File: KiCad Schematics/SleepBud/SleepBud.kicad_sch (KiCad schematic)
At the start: 159 parts, among them J1 12V Barrel Jack, J2 USB_B_Micro, J3 Button Connector, J4 AM312 Connector, J5 LED Lamp Connector, J6 Connector to Buzzer, Q1 FQP27P06, Q2 AO3400A, SW1 EN Button, SW2 Reset Button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

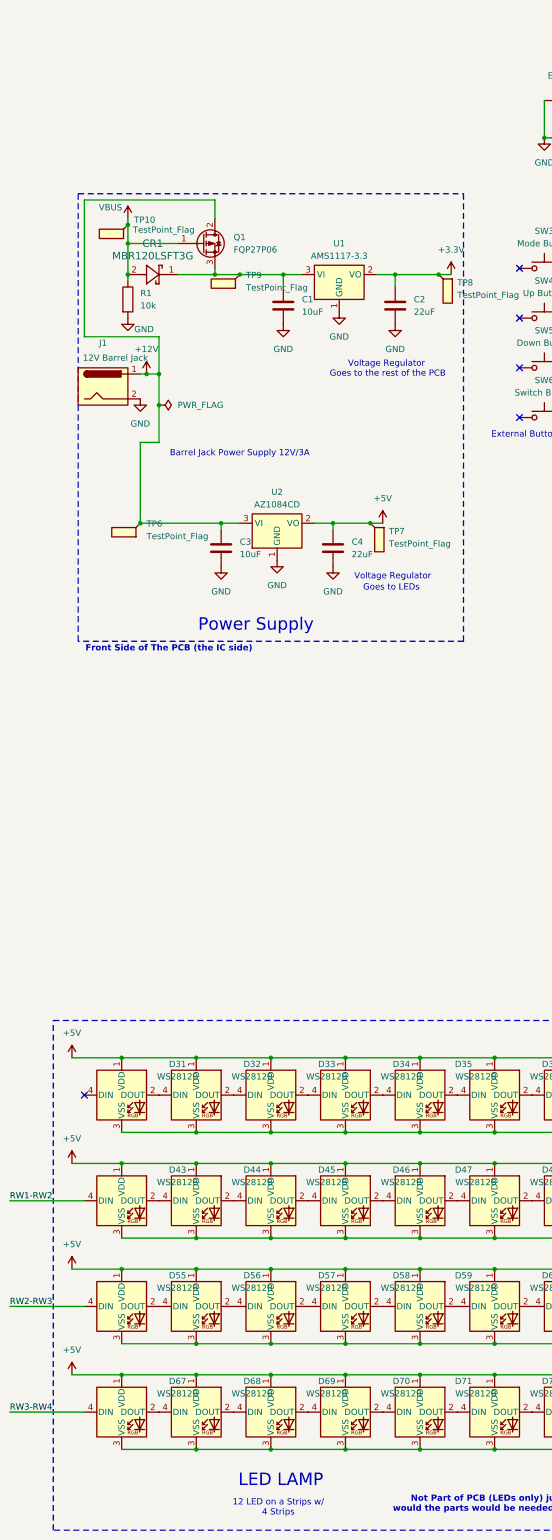
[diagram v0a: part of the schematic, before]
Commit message: Changed PMosfet
Change the Mosfet can be seen on schematic and PCB layout
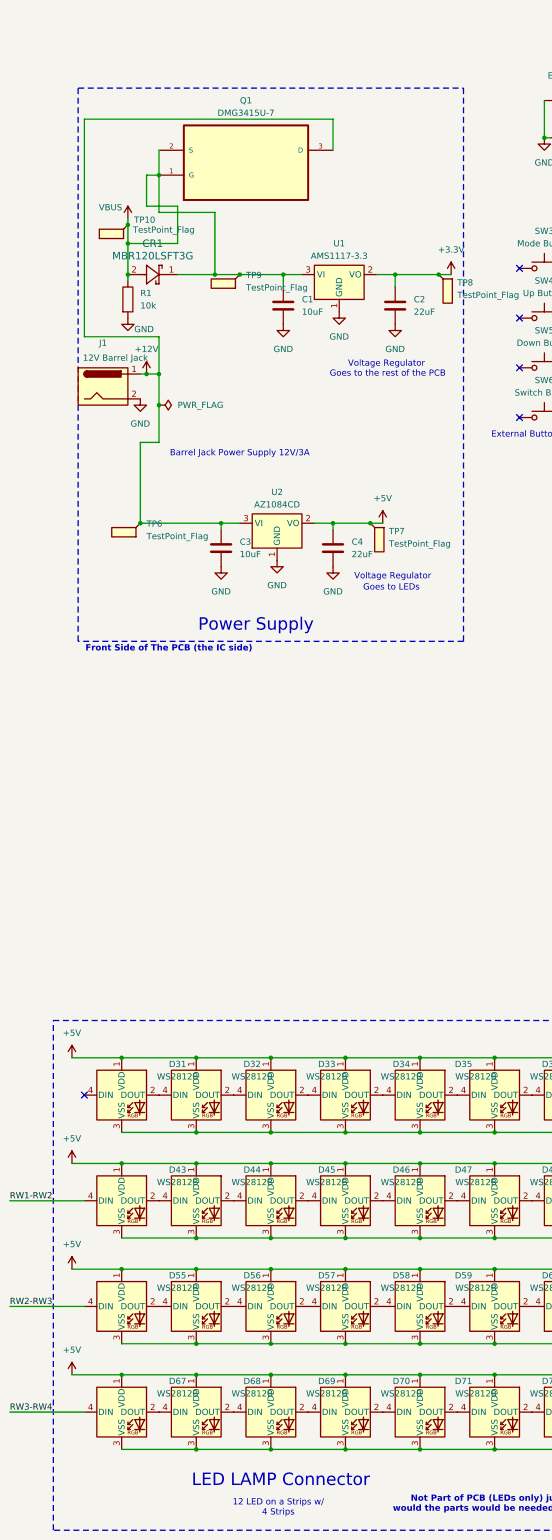
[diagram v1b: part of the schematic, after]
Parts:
- removed Q1: FQP27P06, Package_TO_SOT_THT:TO-220-3_Vertical, symbol Transistor_FET:FQP27P06
- added Q1: DMG3415U-7, DMG3415U_7:SOT95P240X105-3N, symbol DMG3415U-7:DMG3415U-7
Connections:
- net +12V: now also Q1.3 (D)
- net VBUS: now also C1.1, CR1.1, TP9.1, U1.3 (VI), Q1.1 (G), Q1.2 (S)
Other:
- note added: "LED LAMP Connector"
- note removed: "LED LAMP"
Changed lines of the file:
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@@
 	)
 	(junction
+		(at 46.99 125.73)
+		(diameter 0)
+		(color 0 0 0 0)
+	)
+	(junction
 		(at 152.4 91.44)
 		(diameter 0)
@@
 	(wire
 		(pts
+			(xy 50.8 132.08) (xy 44.45 132.08)
+		)
+		(stroke
+			(width 0)
+			(type default)
+		)
+	)
+	(wire
+		(pts
 			(xy 504.19 316.23) (xy 519.43 316.23)
 		)
@@
 	(wire
 		(pts
-			(xy 31.75 158.75) (xy 31.75 130.81)
-		)
-		(stroke
-			(width 0)
-			(type default)
-		)
-	)
-	(wire
-		(pts
 			(xy 58.42 146.05) (xy 63.5 146.05)
 		)
@@
 	(wire
 		(pts
+			(xy 31.75 114.3) (xy 82.55 114.3)
+		)
+		(stroke
+			(width 0)
+			(type default)
+		)
+	)
+	(wire
+		(pts
 			(xy 316.23 200.66) (xy 303.53 200.66)
 		)
@@
 	(wire
 		(pts
-			(xy 31.75 130.81) (xy 58.42 130.81)
+			(xy 302.26 198.12) (xy 302.26 207.01)
 		)
 		(stroke
@@
 	(wire
 		(pts
-			(xy 302.26 198.12) (xy 302.26 207.01)
+			(xy 100.33 342.9) (xy 115.57 342.9)
 		)
 		(stroke
@@
 	(wire
 		(pts
-			(xy 100.33 342.9) (xy 115.57 342.9)
+			(xy 161.29 349.25) (xy 176.53 349.25)
 		)
 		(stroke
@@
 	(wire
 		(pts
-			(xy 161.29 349.25) (xy 176.53 349.25)
+			(xy 58.42 133.35) (xy 58.42 146.05)
 		)
 		(stroke
@@
 	(wire
 		(pts
+			(xy 46.99 133.35) (xy 58.42 133.35)
+		)
+		(stroke
+			(width 0)
+			(type default)
+		)
+	)
+	(wire
+		(pts
 			(xy 46.99 158.75) (xy 31.75 158.75)
 		)
@@
 	(wire
 		(pts
+			(xy 44.45 132.08) (xy 44.45 125.73)
+		)
+		(stroke
+			(width 0)
+			(type default)
+		)
+	)
+	(wire
+		(pts
 			(xy 323.85 171.45) (xy 323.85 180.34)
 		)
@@
 	(wire
 		(pts
+			(xy 46.99 120.65) (xy 46.99 125.73)
+		)
+		(stroke
+			(width 0)
+			(type default)
+		)
+	)
+	(wire
+		(pts
 			(xy 137.16 110.49) (xy 139.7 110.49)
 		)
@@
 	(wire
 		(pts
+			(xy 44.45 125.73) (xy 46.99 125.73)
+		)
+		(stroke
+			(width 0)
+			(type default)
+		)
+	)
+	(wire
+		(pts
 			(xy 229.87 147.32) (xy 248.92 147.32)
 		)
@@
 	(wire
 		(pts
+			(xy 31.75 114.3) (xy 31.75 158.75)
+		)
+		(stroke
+			(width 0)
+			(type default)
+		)
+	)
+	(wire
+		(pts
 			(xy 130.81 327.66) (xy 146.05 327.66)
 		)
@@
 	(wire
 		(pts
-			(xy 220.98 176.53) (xy 220.98 138.43)
+			(xy 50.8 139.7) (xy 50.8 132.08)
 		)
 		(stroke
@@
 	(wire
 		(pts
-			(xy 213.36 115.57) (xy 213.36 92.71)
+			(xy 220.98 176.53) (xy 220.98 138.43)
 		)
 		(stroke
@@
 	(wire
 		(pts
-			(xy 336.55 200.66) (xy 364.49 200.66)
+			(xy 213.36 115.57) (xy 213.36 92.71)
 		)
 		(stroke
@@
 	(wire
 		(pts
-			(xy 58.42 144.78) (xy 58.42 146.05)
+			(xy 336.55 200.66) (xy 364.49 200.66)
 		)
 		(stroke
@@
 	(wire
 		(pts
-			(xy 69.85 349.25) (xy 85.09 349.25)
+			(xy 46.99 125.73) (xy 46.99 133.35)
 		)
 		(stroke
@@
 	(wire
 		(pts
-			(xy 157.48 133.35) (xy 157.48 152.4)
+			(xy 69.85 349.25) (xy 85.09 349.25)
 		)
 		(stroke
@@
 	(wire
 		(pts
-			(xy 180.34 200.66) (xy 180.34 156.21)
+			(xy 157.48 133.35) (xy 157.48 152.4)
 		)
 		(stroke
@@
 	(wire
 		(pts
-			(xy 443.23 300.99) (xy 458.47 300.99)
+			(xy 180.34 200.66) (xy 180.34 156.21)
 		)
 		(stroke
@@
 	(wire
 		(pts
-			(xy 213.36 199.39) (xy 218.44 199.39)
+			(xy 443.23 300.99) (xy 458.47 300.99)
 		)
 		(stroke
@@
 	(wire
 		(pts
-			(xy 427.99 300.99) (xy 443.23 300.99)
+			(xy 213.36 199.39) (xy 218.44 199.39)
 		)
 		(stroke
@@
 	(wire
 		(pts
-			(xy 248.92 154.94) (xy 248.92 151.13)
+			(xy 427.99 300.99) (xy 443.23 300.99)
 		)
 		(stroke
@@
 	(wire
 		(pts
-			(xy 58.42 130.81) (xy 58.42 134.62)
+			(xy 248.92 154.94) (xy 248.92 151.13)
 		)
 		(stroke
@@
 	(wire
 		(pts
+			(xy 82.55 114.3) (xy 82.55 120.65)
+		)
+		(stroke
+			(width 0)
+			(type default)
+		)
+	)
+	(wire
+		(pts
 			(xy 219.71 140.97) (xy 219.71 187.96)
 		)
@@
 	)
 	(rectangle
-		(start 30.48 129.54)
+		(start 30.48 107.95)
 		(end 109.22 220.98)
 		(stroke
@@
 		)
 	)
-	(text "LED LAMP"
+	(text "LED LAMP Connector"
 		(exclude_from_sim no)
 		(at 71.882 392.43 0)
@@
 	)
 	(symbol
-		(lib_id "Transistor_FET:FQP27P06")
-		(at 55.88 139.7 0)
-		(unit 1)
-		(exclude_from_sim no)
-		(in_bom yes)
-		(on_board yes)
-		(dnp no)
-		(fields_autoplaced yes)
-		(property "Reference" "Q1"
-			(at 62.23 138.4299 0)
-			(effects
-				(font
-					(size 1.27 1.27)
-				)
-				(justify left)
-			)
-		)
-		(property "Value" "FQP27P06"
-			(at 62.23 140.9699 0)
-			(effects
-				(font
-					(size 1.27 1.27)
-				)
-				(justify left)
-			)
-		)
-		(property "Footprint" "Package_TO_SOT_THT:TO-220-3_Vertical"
-			(at 60.96 141.605 0)
-			(effects
-				(font
-					(size 1.27 1.27)
-					(italic yes)
-				)
-				(justify left)
-				(hide yes)
-			)
-		)
-		(property "Datasheet" "https://www.onsemi.com/pub/Collateral/FQP27P06-D.PDF"
-			(at 60.96 143.51 0)
-			(effects
-				(font
-					(size 1.27 1.27)
-				)
-				(justify left)
-				(hide yes)
-			)
-		)
-		(property "Description" "-27A Id, -60V Vds, QFET P-Channel MOSFET, TO-220"
-			(at 55.88 139.7 0)
-			(effects
-				(font
-					(size 1.27 1.27)
-				)
-				(hide yes)
-			)
-		)
-		(pin "1"
-		)
-		(pin "3"
-		)
-		(pin "2"
-		)
-		(instances
-			(project ""
-				(path "/976e55d6-47c8-4a6a-a3ac-d81121411704"
-					(reference "Q1")
-					(unit 1)
-				)
-			)
-		)
-	)
-	(symbol
 		(lib_id "JTAG Pads:JTAG_PAD")
 		(at 224.79 187.96 0)
@@
 					(unit 1)
 				)
+			)
+		)
+	)
+	(symbol
+		(lib_id "DMG3415U-7:DMG3415U-7")
+		(at 64.77 120.65 0)
+		(unit 1)
+		(exclude_from_sim no)
+		(in_bom yes)
+		(on_board yes)
+		(dnp no)
+		(fields_autoplaced yes)
+		(property "Reference" "Q1"
+			(at 64.77 110.49 0)
+			(effects
+				(font
+					(size 1.27 1.27)
+				)
+			)
+		)
+		(property "Value" "DMG3415U-7"
+			(at 64.77 113.03 0)
+			(effects
+				(font
+					(size 1.27 1.27)
+				)
+			)
+		)
+		(property "Footprint" "DMG3415U_7:SOT95P240X105-3N"
+			(at 64.77 120.65 0)
+			(effects
+				(font
+					(size 1.27 1.27)
+				)
+				(justify bottom)
+				(hide yes)
+			)
+		)
+		(property "Datasheet" ""
+			(at 64.77 120.65 0)
+			(effects
+				(font
+					(size 1.27 1.27)
+				)
+				(hide yes)
+			)
+		)
+		(property "Description" ""
+			(at 64.77 120.65 0)
+			(effects
+				(font
+					(size 1.27 1.27)
+				)
+				(hide yes)
+			)
+		)
+		(property "MPN" "DMG3415U-7"
+			(at 64.77 120.65 0)
+			(effects
+				(font
+					(size 1.27 1.27)
+				)
+				(justify bottom)
+				(hide yes)
+			)
+		)
+		(property "OC_FARNELL" "1843688"
+			(at 64.77 120.65 0)
+			(effects
+				(font
+					(size 1.27 1.27)
+				)
+				(justify bottom)
+				(hide yes)
+			)
+		)
+		(property "OC_NEWARK" "12T2026"
+			(at 64.77 120.65 0)
+			(effects
+				(font
+					(size 1.27 1.27)
+				)
+				(justify bottom)
+				(hide yes)
+			)
+		)
+		(property "SUPPLIER" "Diodes Inc"
+			(at 64.77 120.65 0)
+			(effects
+				(font
+					(size 1.27 1.27)
+				)
+				(justify bottom)
+				(hide yes)
+			)
+		)
+		(property "PACKAGE" "SOT-23-3"
+			(at 64.77 120.65 0)
+			(effects
+				(font
+					(size 1.27 1.27)
+				)
+				(justify bottom)
+				(hide yes)
+			)
+		)
+		(pin "3"
+		)
+		(pin "1"
+		)
+		(pin "2"
+		)
+		(instances
+			(project ""
+				(path "/976e55d6-47c8-4a6a-a3ac-d81121411704"
+					(reference "Q1")
+					(unit 1)
+				)

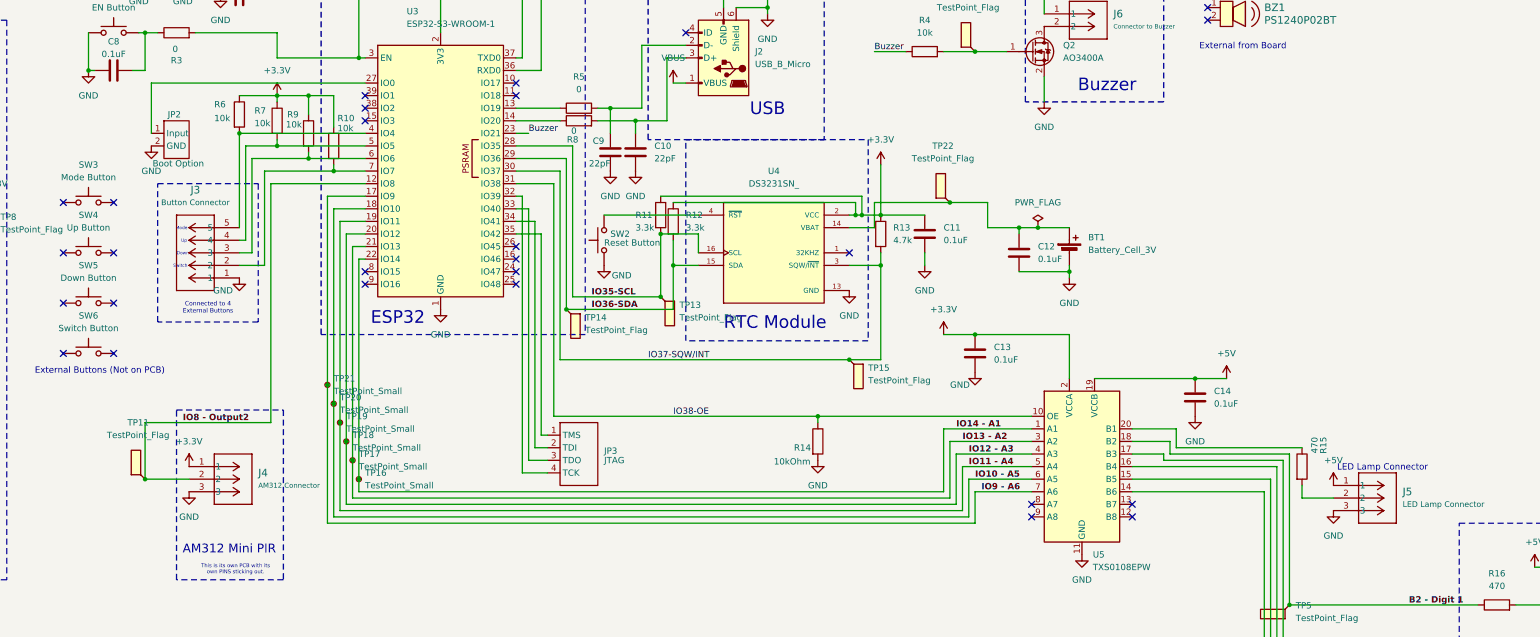
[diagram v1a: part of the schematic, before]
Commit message: Added Some Ground Vias to each Corner of the Board
Still missing the ground stitching for some components, will work on it it later
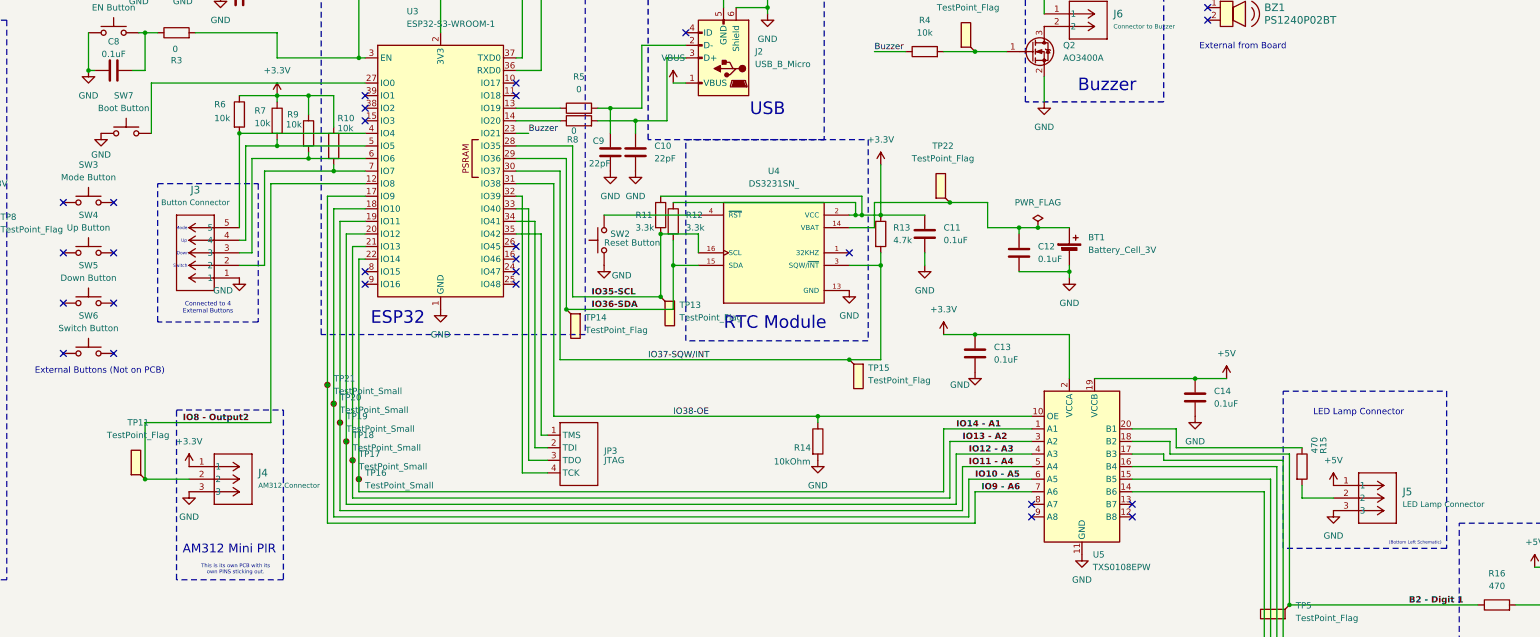
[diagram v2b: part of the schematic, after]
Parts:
- removed JP2: Boot Option, Connector_PinHeader_1.00mm:PinHeader_2x01_P1.00mm_Vertical_SMD, symbol Boot Option:Boot_Option
- added SW7: Boot Button, Button_Switch_SMD:SW_Tactile_SPST_NO_Straight_CK_PTS636Sx25SMTRLFS, symbol Switch:SW_Push
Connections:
- net GND: now also SW7.1
- net at U3.27 (IO0): now also SW7.2
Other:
- note added: "(Bottom Left Schematic)"
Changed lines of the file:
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@@
 	)
 	(rectangle
+		(start 367.03 182.88)
+		(end 400.05 214.63)
+		(stroke
+			(width 0)
+			(type dash_dot)
+		)
+		(fill
+			(type none)
+		)
+	)
+	(rectangle
 		(start 246.38 132.08)
 		(end 283.21 172.72)
@@
 	(text "LED Lamp Connector\n"
 		(exclude_from_sim no)
-		(at 387.096 198.374 0)
+		(at 382.27 187.198 0)
 		(effects
 			(font
@@
 		)
 	)
+	(text "(Bottom Left Schematic)"
+		(exclude_from_sim no)
+		(at 393.7 213.614 0)
+		(effects
+			(font
+				(size 0.635 0.635)
+			)
+		)
+	)
 	(text "ESP32"
 		(exclude_from_sim no)
@@
 	(symbol
 		(lib_id "power:GND")
-		(at 138.43 133.35 0)
+		(at 128.27 130.81 0)
 		(unit 1)
 		(exclude_from_sim no)
@@
 		(on_board yes)
 		(dnp no)
-		(fields_autoplaced yes)
 		(property "Reference" "#PWR024"
-			(at 138.43 139.7 0)
+			(at 128.27 137.16 0)
 			(effects
 				(font
@@
 		)
 		(property "Value" "GND"
-			(at 138.43 138.43 0)
+			(at 128.27 135.128 0)
 			(effects
 				(font
@@
 		)
 		(property "Footprint" ""
-			(at 138.43 133.35 0)
+			(at 128.27 130.81 0)
 			(effects
 				(font
@@
 		)
 		(property "Datasheet" ""
-			(at 138.43 133.35 0)
+			(at 128.27 130.81 0)
 			(effects
 				(font
@@
 		)
 		(property "Description" "Power symbol creates a global label with name \"GND\" , ground"
-			(at 138.43 133.35 0)
+			(at 128.27 130.81 0)
 			(effects
 				(font
@@
 	)
 	(symbol
+		(lib_id "Switch:SW_Push")
+		(at 133.35 130.81 0)
+		(unit 1)
+		(exclude_from_sim no)
+		(in_bom yes)
+		(on_board yes)
+		(dnp no)
+		(property "Reference" "SW7"
+			(at 132.842 123.19 0)
+			(effects
+				(font
+					(size 1.27 1.27)
+				)
+			)
+		)
+		(property "Value" "Boot Button"
+			(at 132.842 125.73 0)
+			(effects
+				(font
+					(size 1.27 1.27)
+				)
+			)
+		)
+		(property "Footprint" "Button_Switch_SMD:SW_Tactile_SPST_NO_Straight_CK_PTS636Sx25SMTRLFS"
+			(at 133.35 125.73 0)
+			(effects
+				(font
+					(size 1.27 1.27)
+				)
+				(hide yes)
+			)
+		)
+		(property "Datasheet" "~"
+			(at 133.35 125.73 0)
+			(effects
+				(font
+					(size 1.27 1.27)
+				)
+				(hide yes)
+			)
+		)
+		(property "Description" "Push button switch, generic, two pins"
+			(at 133.35 130.81 0)
+			(effects
+				(font
+					(size 1.27 1.27)
+				)
+				(hide yes)
+			)
+		)
+		(pin "1"
+		)
+		(pin "2"
+		)
+		(instances
+			(project "SleepBud"
+				(path "/976e55d6-47c8-4a6a-a3ac-d81121411704"
+					(reference "SW7")
+					(unit 1)
+				)
+			)
+		)
+	)
+	(symbol
 		(lib_id "power:GND")
 		(at 304.8 179.07 0)
@@
 					(unit 1)
 				)
-			)
-		)
-	)
-	(symbol
-		(lib_id "Boot Option:Boot_Option")
-		(at 143.51 127 0)
-		(unit 1)
-		(exclude_from_sim no)
-		(in_bom yes)
-		(on_board yes)
-		(dnp no)
-		(property "Reference" "JP2"
-			(at 141.732 127 0)
-			(effects
-				(font
-					(size 1.27 1.27)
-				)
-				(justify left)
-			)
-		)
-		(property "Value" "Boot Option"
-			(at 138.684 136.906 0)
-			(effects
-				(font
-					(size 1.27 1.27)
-				)
-				(justify left)
-			)
-		)
-		(property "Footprint" "Connector_PinHeader_1.00mm:PinHeader_2x01_P1.00mm_Vertical_SMD"
-			(at 143.51 127 0)
-			(effects
-				(font
-					(size 1.27 1.27)
-				)
-				(hide yes)
-			)
-		)
-		(property "Datasheet" ""
-			(at 143.51 127 0)
-			(effects
-				(font
-					(size 1.27 1.27)
-				)
-				(hide yes)
-			)
-		)
-		(property "Description" ""
-			(at 143.51 127 0)
-			(effects
-				(font
-					(size 1.27 1.27)
-				)
-				(hide yes)
-			)
-		)
-		(pin "2"
-		)
-		(pin "1"
-		)
-		(instances
-			(project ""
-				(path "/976e55d6-47c8-4a6a-a3ac-d81121411704"
-					(reference "JP2")
-					(unit 1)
-				)

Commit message: Finished PCB V1.5
Added LEDs to see if PCB is getting power

Changed TestPoint sizes

Added more grounds to even out board
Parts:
- added D79, D80: WL-SMCW_0603, 150060RS75000:WL-SMCW_0603, symbol WL-SMCW_0603:WL-SMCW_0603
- added R21: 100, Resistor_SMD:R_0805_2012Metric, symbol Device:R
- added R22: 180, Resistor_SMD:R_0805_2012Metric, symbol Device:R
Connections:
- net +3.3V: now also R21.2
- net +5V: now also R22.2
- net GND: now also D79.1, D80.1
- net VBUS: no longer C1.1, CR1.1, Q1.2 (S), TP9.1, U1.3 (VI)
- new net: C1.1, CR1.1, Q1.2 (S), TP9.1, U1.3 (VI)
- new net: D80.2, R21.1
- new net: D79.2, R22.1
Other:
- note added: "Version 1.4"
- note removed: "Version 1.3"

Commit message: Final PCB
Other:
- note added: "11/20/2024"
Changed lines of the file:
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@@
+		)
+	)
+	(text "11/20/2024"
+		(exclude_from_sim no)
+		(at 509.778 403.352 0)
+		(effects
+			(font
+				(size 1.27 1.27)
+				(thickness 0.254)
+				(bold yes)
+			)
 		)
 	)

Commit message: changed schematic from 12v/3a to 7v 3a
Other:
- note added: "12/01/2024"
- note added: "Barrel Jack Power Supply 7V/3A"
- note added: "Version 1.5"
- note removed: "11/20/2024"
- note removed: "Barrel Jack Power Supply 12V/3A"
- note removed: "Version 1.4"
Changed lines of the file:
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@@
 		)
 	)
-	(text "Barrel Jack Power Supply 12V/3A"
+	(text "Barrel Jack Power Supply 7V/3A"
 		(exclude_from_sim no)
 		(at 63.5 182.626 0)
@@
 		)
 	)
-	(text "11/20/2024"
+	(text "12/01/2024"
 		(exclude_from_sim no)
 		(at 509.778 403.352 0)
@@
 		)
 	)
-	(text " Version 1.4\n"
+	(text " Version 1.5\n"
 		(exclude_from_sim no)
 		(at 506.73 400.05 0)

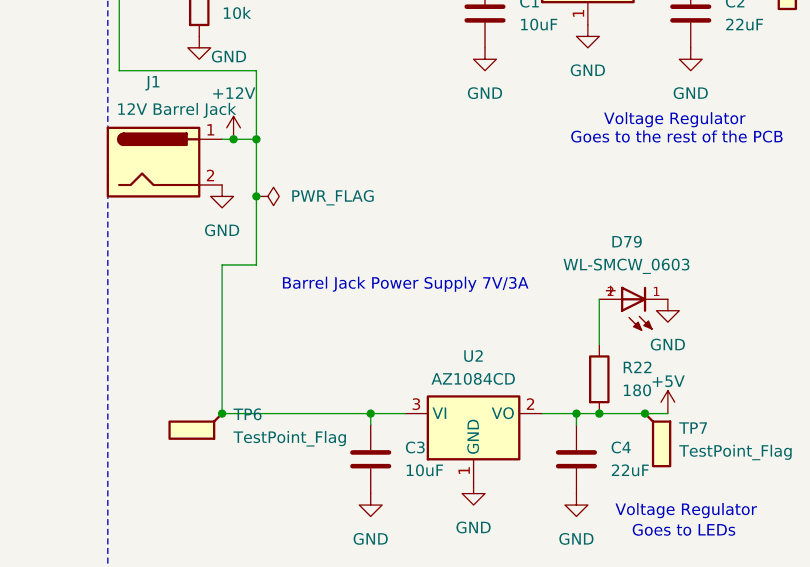
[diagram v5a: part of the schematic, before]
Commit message: wrote 7v instead of 9v on schematic
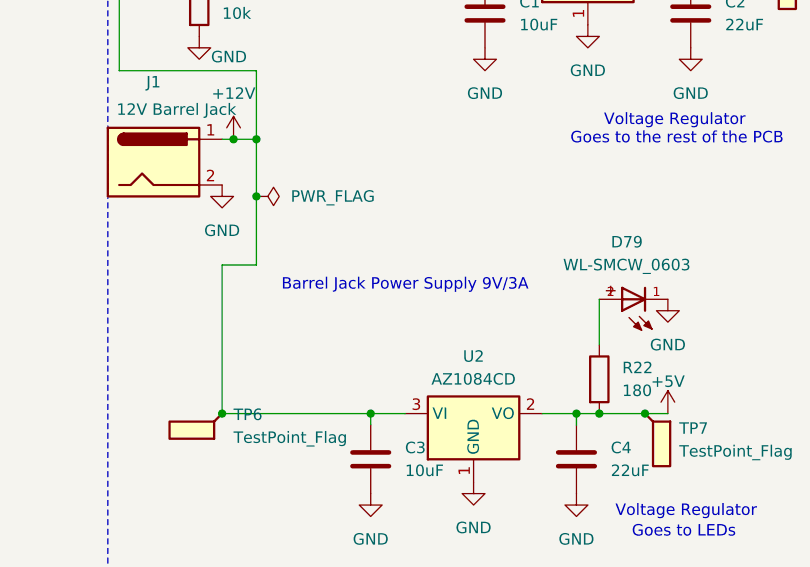
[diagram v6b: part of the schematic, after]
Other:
- note added: "Barrel Jack Power Supply 9V/3A"
- note removed: "Barrel Jack Power Supply 7V/3A"
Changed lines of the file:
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@@
 		)
 	)
-	(text "Barrel Jack Power Supply 7V/3A"
+	(text "Barrel Jack Power Supply 9V/3A"
 		(exclude_from_sim no)
 		(at 63.5 182.626 0)
